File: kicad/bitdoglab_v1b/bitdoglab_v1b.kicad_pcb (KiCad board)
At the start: 2 copper layers, 87.9 x 123.9 mm, 45 parts, among them J1 conector_idc, J10 Conn_01x05_Pin, J11 Conn_01x05_Pin, J12 WS2812 5x5 Matrix led, J13 GP03, J14 GP02, J15 GP01, J16 GP00, J17 JOYSTICK, J2 jumper_mic, J3 Conn_01x05_Pin, J4 Conn_01x05_Pin, J5 GND, J6 GP28, J7 AGND, J8 3.3_OUT, J9 VBUS, Q1 DMG2305UX-13, Q2 BC337, Q3 BC337, SW1 RESET, SW2 Button_A, SW3 Button_B, U1 3.3v_tht, U2 3.3v_smd, U3 BAT (DIS)CHARGE, U4 1063

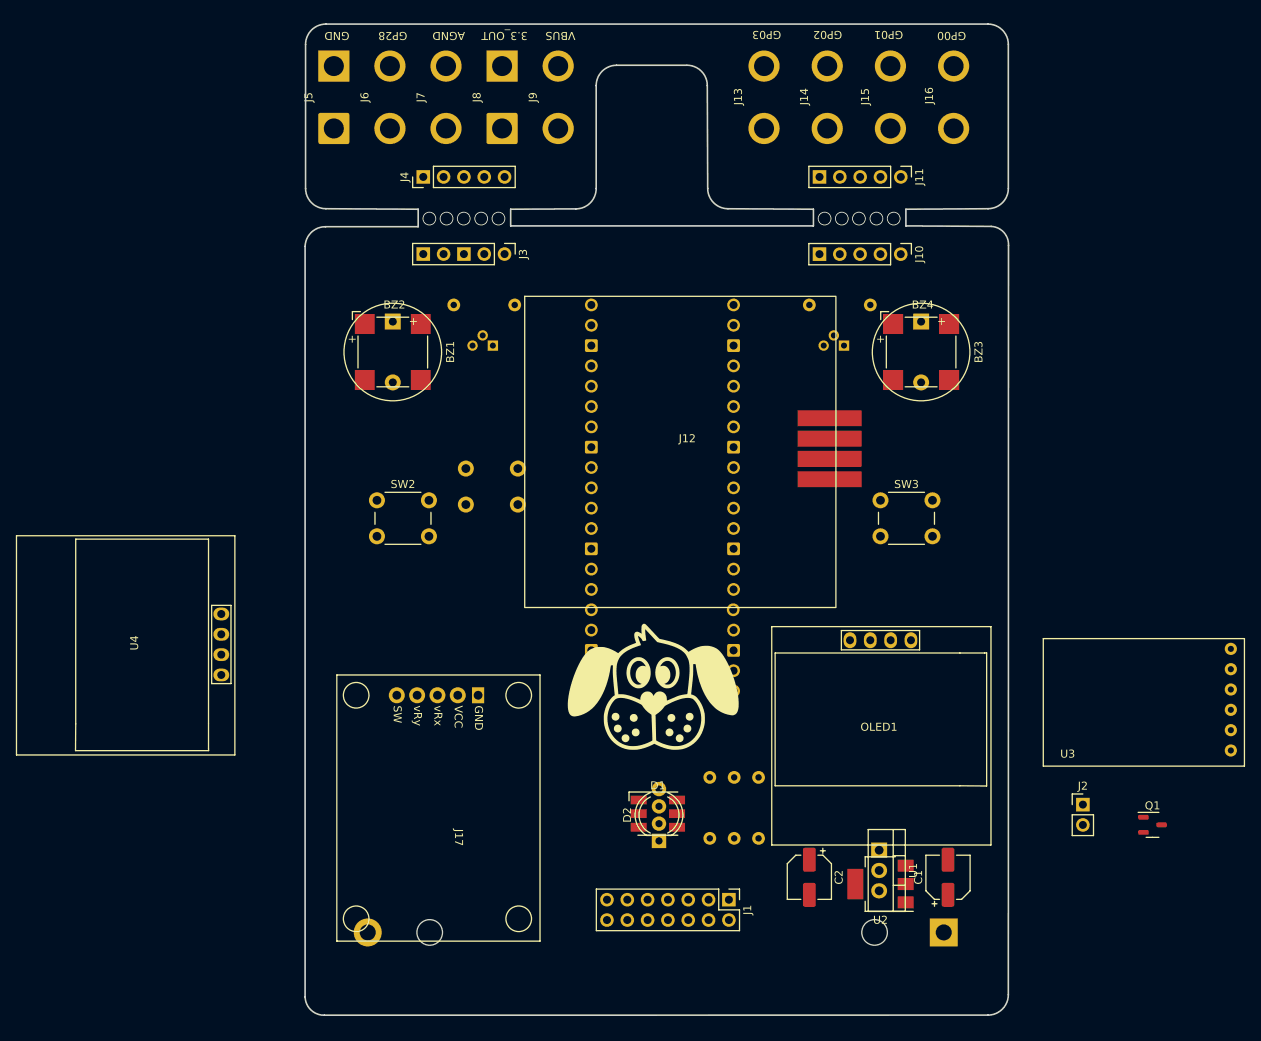
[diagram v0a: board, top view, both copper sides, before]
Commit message: Finalizacao do placement dos componentes
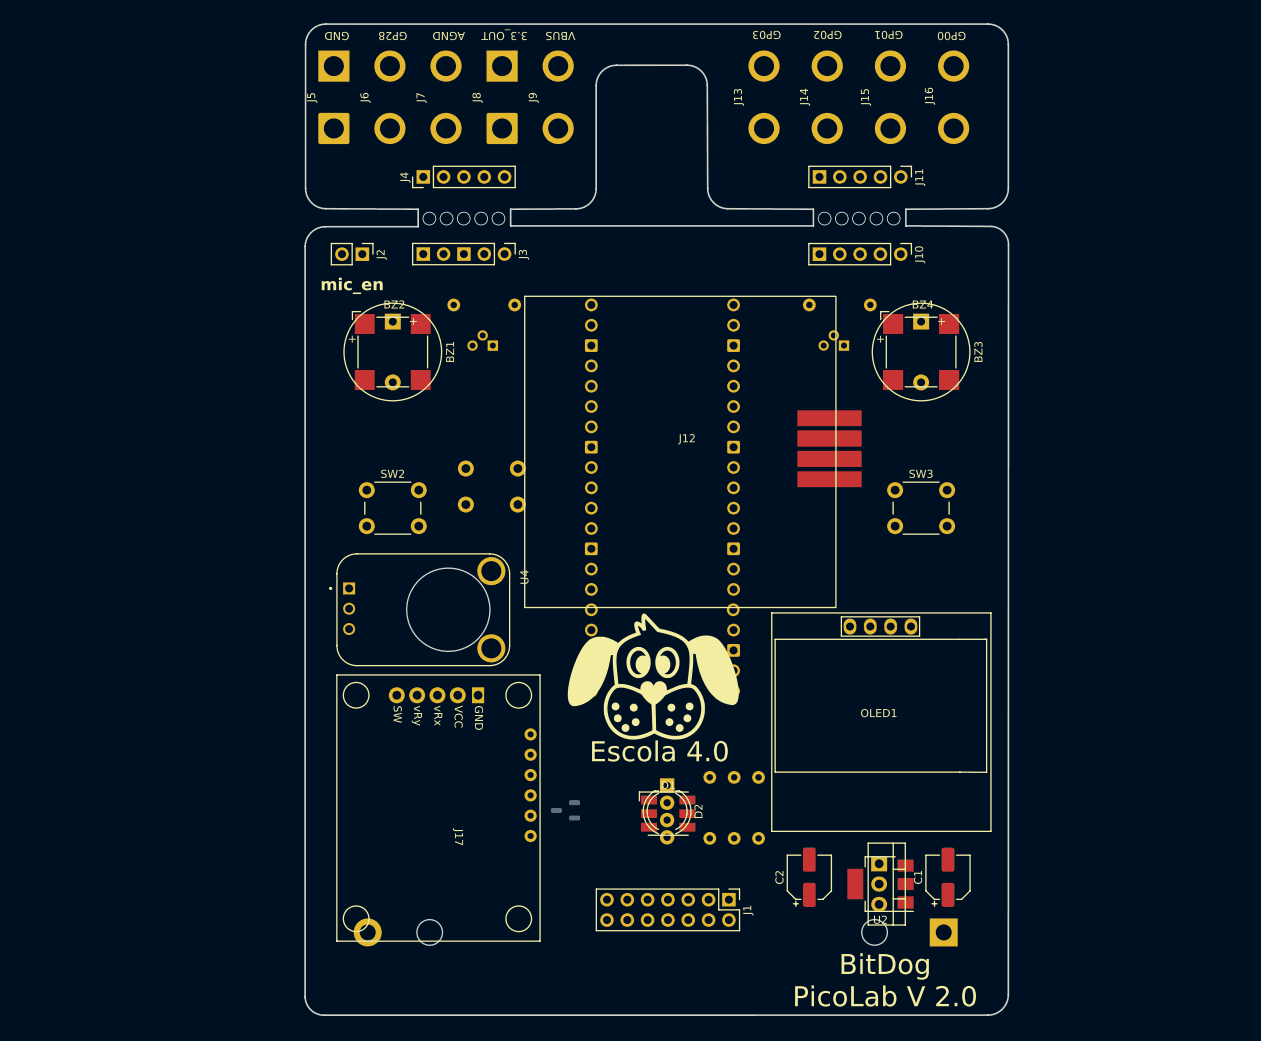
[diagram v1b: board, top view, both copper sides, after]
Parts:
- added G***: LOGO, LOGO, B.Cu at (153.7, 127.0)
- BZ1: value Buzzer_A -> Buzzers_A
- BZ4: value Buzzer_B_SMD -> Buzzers_B
- D2: value LED_BGRK -> LEDS RGB
- J1: value conector_idc -> Connector IDC
- J12: value WS2812 5x5 Matrix led -> 5x5 Matrix led
- J2: value jumper_mic -> mic_en
- OLED1: value SSD1306 -> DISPLAY OLED
- Q1, U3: moved to B.Cu
- U4: value 1063 -> Microphone; footprint user_SSD1306:128x64OLED -> user_1063:MODULE_1063
- moved J2 113.3 mm to (95.2, 61.0), turned to -90 degrees
- moved U3 87.7 mm to (93.0, 119.3)
- moved Q1 73.4 mm to (120.7, 130.5), turned to 180 degrees
- moved G*** 45.2 mm to (163.4, 100.3), turned to -90 degrees
- moved U4 36.1 mm to (102.9, 105.4)
- moved D2 7.00 mm to (133.3, 127.4), turned to -90 degrees
- moved SW3 2.23 mm to (161.8, 90.5)
- moved SW2 1.80 mm to (95.8, 90.5)
- moved OLED1 1.71 mm to (159.8, 118.1)
- moved U1 1.70 mm to (159.9, 137.2)
- moved D1 1.30 mm to (133.5, 130.9)
- moved G*** 1.28 mm to (131.8, 114.3)
- turned C2 to 90 degrees
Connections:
- A1 pad 37: +3.3V -> unconnected-(A1-3V3_EN-Pad37)
- BZ1 pad 1: VBUS -> VSYS
- BZ2 pad 1: VBUS -> VSYS
- BZ3 pad 1: VBUS -> VSYS
- BZ4 pad 1: VBUS -> VSYS
- C1 pad 1: VBUS -> VSYS
- D1 pad 5: Net-(D1-GA) -> Net-(D1-BA)
- D1 pad 6: Net-(D1-RA) -> Net-(D1-BA)
- D2 pad 2: Net-(D1-GA) -> GNDREF
- D2 pad 3: Net-(D1-RA) -> Net-(D1-BA)
- D2 pad 4: GNDREF -> Net-(D1-BA)
- J12 pad 3: VBUS -> VSYS
- J17 pad 2: VBUS -> 3.3_OUT
- Rg1 pad 1: Net-(D1-GA) -> Net-(D1-BA)
- Rr1 pad 1: Net-(D1-RA) -> Net-(D1-BA)
- SW1 pad 1: GNDREF -> Net-(A1-RUN)
- SW1 pad 2: Net-(A1-RUN) -> GNDREF
- SW2 pad 1: GNDREF -> Net-(A1-GP5)
- SW2 pad 2: Net-(A1-GP5) -> GNDREF
- SW3 pad 1: GNDREF -> Net-(A1-GP6)
- SW3 pad 2: Net-(A1-GP6) -> GNDREF
- U1 pad 3: VBUS -> VSYS
- U2 pad 1: VBUS -> VSYS
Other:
- outline, holes or cut-outs redrawn
- board text added: "BitDog PicoLab V 2.0"
- board text added: "Escola 4.0"

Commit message: roteamento e apagando backups
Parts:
- added J1: Conn_01x20_Socket, Connector_PinHeader_2.54mm:PinHeader_1x20_P2.54mm_Vertical, B.Cu at (146.1, 67.3)
- added J3: Conn_01x20_Socket, Connector_PinHeader_2.54mm:PinHeader_1x20_P2.54mm_Vertical, B.Cu at (119.4, 115.5)
- BZ1: value Buzzers_A -> Buzzer_A
- BZ4: value Buzzers_B -> Buzzer_B_SMD
- D2: value LEDS RGB -> LED_RAGB
- J2: renamed from J1; value Connector IDC -> conector_idc
- J4: renamed from J2; value mic_en -> jumper_mic
- OLED1: value DISPLAY OLED -> SSD1306
- U4: value Microphone -> 1063
- moved Q1 6.40 mm to (120.1, 124.1), turned to -90 degrees
- moved OLED1 1.19 mm to (161.0, 118.1)
- renumbered G*** to G1, G*** to G2, G*** to G3, J8 to J10, J9 to J11, J10 to J12, J11 to J13, J12 to J14, J13 to J15, J14 to J16, J15 to J17, J16 to J18, J17 to J19, J3 to J5, J4 to J6, J5 to J7, J6 to J8, J7 to J9
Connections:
- net /sw renamed /pino_29
- net /vrx renamed /pino_31
- net /vry renamed /pino_32
- net Net-(A1-GP14) renamed /pino_19
- net Net-(A1-GP15) renamed /pino_20
- net Net-(A1-GP21) renamed /pino_27
- net Net-(A1-GP5) renamed /pino_07
- net Net-(A1-GP6) renamed /pino_09
- net Net-(A1-RUN) renamed /pino_30
- A1 pad 37: unconnected-(A1-3V3_EN-Pad37) -> /pino_37
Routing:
- net VSYS: track 0.00 -> 230.4 mm
- net VBUS: track 0.00 -> 160.3 mm
- net 3.3_OUT: track 0.00 -> 121.5 mm
- net +3.3V: track 0.00 -> 115.0 mm, vias 0 -> 1
- net /GP28: track 0.00 -> 113.2 mm
- net /GP09: track 0.00 -> 64.4 mm, vias 0 -> 1
- net /GP08: track 0.00 -> 61.6 mm, vias 0 -> 1
- net Net-(BT1-+): track 0.00 -> 60.8 mm
- net /GP10: track 0.00 -> 60.0 mm, vias 0 -> 1
- net /GP20: track 0.00 -> 57.5 mm
- net /pino_32: track 0.00 -> 53.9 mm
- net /pino_07: track 0.00 -> 53.6 mm
- net /GP19: track 0.00 -> 45.8 mm
- net /GP18: track 0.00 -> 44.1 mm
- net /pino_31: track 0.00 -> 43.6 mm
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- added copper zone on B.Cu, net GNDREF
- added copper zone on F.Cu, net GNDREF
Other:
- outline, holes or cut-outs redrawn
- board text added: "BitDog PicoLab V2.0"
- board text removed: "BitDog PicoLab V 2.0"

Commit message: Ajustes no roteamento
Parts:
- J10: value 3.3_OUT -> GND
- J11: value VBUS -> GND
- J15: value GP03 -> GND
- J16: value GP02 -> GND
- J17: value GP01 -> GND
- J18: value GP00 -> GND
- J8: value GP28 -> GND
- J9: value AGND -> GND
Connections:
- D1 pad 5: Net-(D1-BA) -> Net-(D1-GA)
- D1 pad 6: Net-(D1-BA) -> Net-(D1-RA)
- D2 pad 1: Net-(D1-BA) -> Net-(D1-RA)
- D2 pad 4: Net-(D1-BA) -> Net-(D1-GA)
- J10 pad 2: (no net) -> 3.3_OUT_EXT
- J11 pad 2: (no net) -> VBUS_EXT
- J15 pad 2: (no net) -> /GP03_EXT
- J16 pad 2: (no net) -> /GP02_EXT
- J17 pad 2: (no net) -> /GP01_EXT
- J18 pad 2: (no net) -> /GP0_EXT
- J7 pad 2: (no net) -> GNDREF
- J8 pad 2: (no net) -> /GP28_EXT
- J9 pad 2: (no net) -> /AGND_EXT
- Rg1 pad 1: Net-(D1-BA) -> Net-(D1-GA)
- Rr1 pad 1: Net-(D1-BA) -> Net-(D1-RA)
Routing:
- net VBUS: track 160.3 -> 128.9 mm
- net Net-(Q2-B): track 6.17 -> 26.2 mm
- net Net-(D1-RA): track 0.00 -> 12.0 mm
- net +3.3V: track 115.0 -> 104.5 mm
- net Net-(D1-GA): track 0.00 -> 9.75 mm
- net VSYS: track 230.4 -> 240.0 mm
- net 3.3_OUT_EXT: track 6.98 -> 14.8 mm
- net /GP01_EXT: track 7.63 -> 15.4 mm
- net VBUS_EXT: track 9.57 -> 17.4 mm
- net /GP28_EXT: track 9.81 -> 17.6 mm
- net /GP0_EXT: track 17.1 -> 24.9 mm
- net /GP03_EXT: track 21.8 -> 29.6 mm
- net /AGND_EXT: track 6.98 -> 14.8 mm
- net /GP02_EXT: track 12.7 -> 20.5 mm
- net /GP20: track 57.5 -> 50.1 mm
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
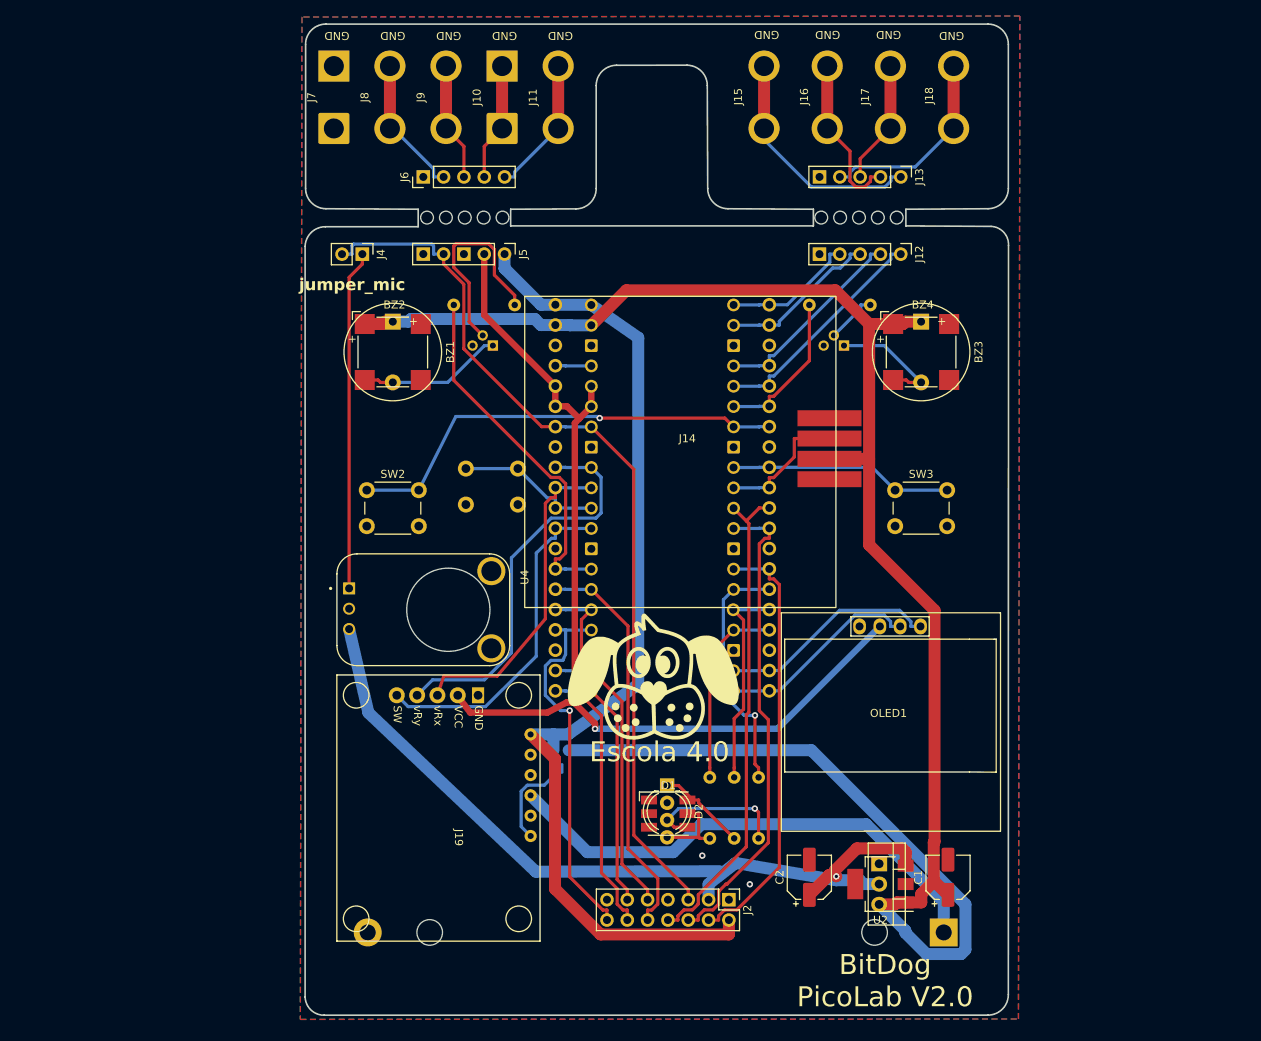
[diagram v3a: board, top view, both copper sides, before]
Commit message: Modificações no layout do professor e envio para confeccao
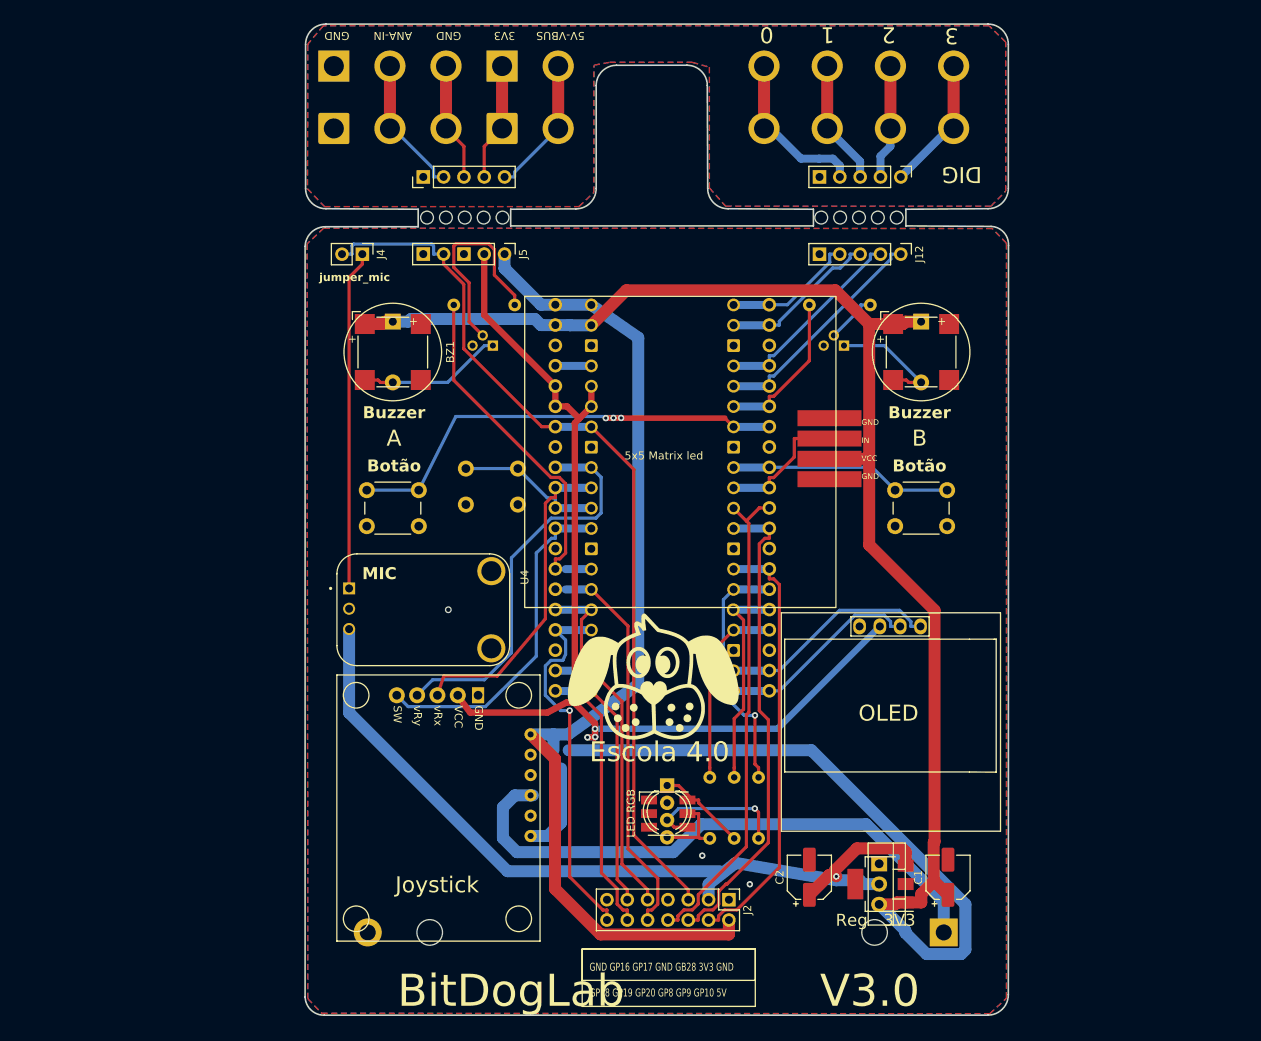
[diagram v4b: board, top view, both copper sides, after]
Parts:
- J10: value GND -> 3V3
- J11: value GND -> 5V-VBUS
- J15: value GND -> 0
- J16: value GND -> 1
- J17: value GND -> 2
- J18: value GND -> 3
- J8: value GND -> ANA-IN
- LED RGB: renamed from D1
- Rb 150: renamed from Rb1
- Reg   3V3: renamed from U2
- Rg 220: renamed from Rg1
- Rr 220: renamed from Rr1
- SW1: value RESET -> Reset
- SW2: value Button_A -> Botão
- U4: value 1063 -> MIC
- moved G2 0.82 mm to (163.7, 101.1)
- renumbered BZ4 to Buzzer, BZ2 to Buzzer, U3 to Charge/DisCharge, OLED1 to OLED
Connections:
- J13 pad 5: GNDREF -> /AGND_EXT
- J15 pad 1: /GP03_EXT -> /GP0_EXT
- J15 pad 2: /GP03_EXT -> /GP0_EXT
- J16 pad 1: /GP02_EXT -> /GP01_EXT
- J16 pad 2: /GP02_EXT -> /GP01_EXT
- J17 pad 1: /GP01_EXT -> /GP02_EXT
- J17 pad 2: /GP01_EXT -> /GP02_EXT
- J18 pad 1: /GP0_EXT -> /GP03_EXT
- J18 pad 2: /GP0_EXT -> /GP03_EXT
- J6 pad 1: GNDREF -> /AGND_EXT
- J7 pad 1: GNDREF -> /AGND_EXT
- J7 pad 2: GNDREF -> /AGND_EXT
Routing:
- net /GP03_EXT: track 29.6 -> 16.9 mm
- net Net-(BT1-+): track 63.9 -> 73.3 mm
- net /GP02_EXT: track 20.5 -> 14.4 mm
- net /pino_07: track 56.5 -> 61.7 mm, vias 1 -> 3
- net /GP0_EXT: track 24.9 -> 20.6 mm
- net 3.3_OUT: track 128.0 -> 132.0 mm, vias 1 -> 3
- net +3.3V: track 104.5 -> 106.9 mm
- net /GP18: track 46.8 -> 48.6 mm
- net /GP01: track 20.1 -> 21.3 mm
- net /pino_37: track 4.51 -> 5.76 mm
- net /pino_31: track 40.3 -> 41.6 mm
- net /pino_29: track 42.4 -> 43.7 mm
- net /pino_09: track 27.9 -> 29.1 mm
- net /in: track 16.6 -> 17.9 mm
- net /GP28: track 112.0 -> 113.2 mm
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- added copper zone on B.Cu, net /AGND_EXT
- added copper zone on F.Cu, net /AGND_EXT
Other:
- outline, holes or cut-outs redrawn
- board text added: "+"
- board text added: "-"
- board text added: "3V3"
- board text added: "A"
- board text added: "B"
- board text added: "BAT"
- board text added: "BC337"
- board text added: "Bateria Li-ion 18650 3.7V"
- board text added: "BitDogLab V3.0"
- board text added: "Botão"
- board text added: "Buzzer"
- board text added: "DIG"
- board text added: "GND"
- board text added: "GND GP16 GP17 GND GB28 3V3 GND GP18 GP19 GP20 GP8 GP9 GP10 5V"
- board text added: "GND IN VCC GND"
- board text added: "Joystick"
- board text added: "MIC"
- board text added: "MOSFET"
- board text added: "OUT"
- board text added: "OUT 5V"
- board text added: "Raspberry PI pico"
- board text added: "VIN"
- board text removed: "BitDog PicoLab V2.0"
